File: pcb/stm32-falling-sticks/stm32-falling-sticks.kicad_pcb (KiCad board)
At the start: 2 copper layers, 112 x 87 mm, 73 parts, among them J1 MAG_01-05_OUT, J10 Barrel_Jack, J11 BUZ_OUT, J2 HAL_01-05_IN, J3 LCD_OUT, J4 MAG_06-10_OUT, J5 HAL_06-10_IN, J6 START_IN, J7 POT_IN, J8 MP1584EN, J9 Screw_Terminal_01x02, Q1 AO3400A, Q10 AO3400A, Q11 AO3400A, Q2 AO3400A, Q3 AO3400A, Q4 AO3400A, Q5 AO3400A, Q6 AO3400A, Q7 AO3400A, Q8 AO3400A, Q9 AO3400A, U1 YAAJ_BluePill_Part_Like_SWD_B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

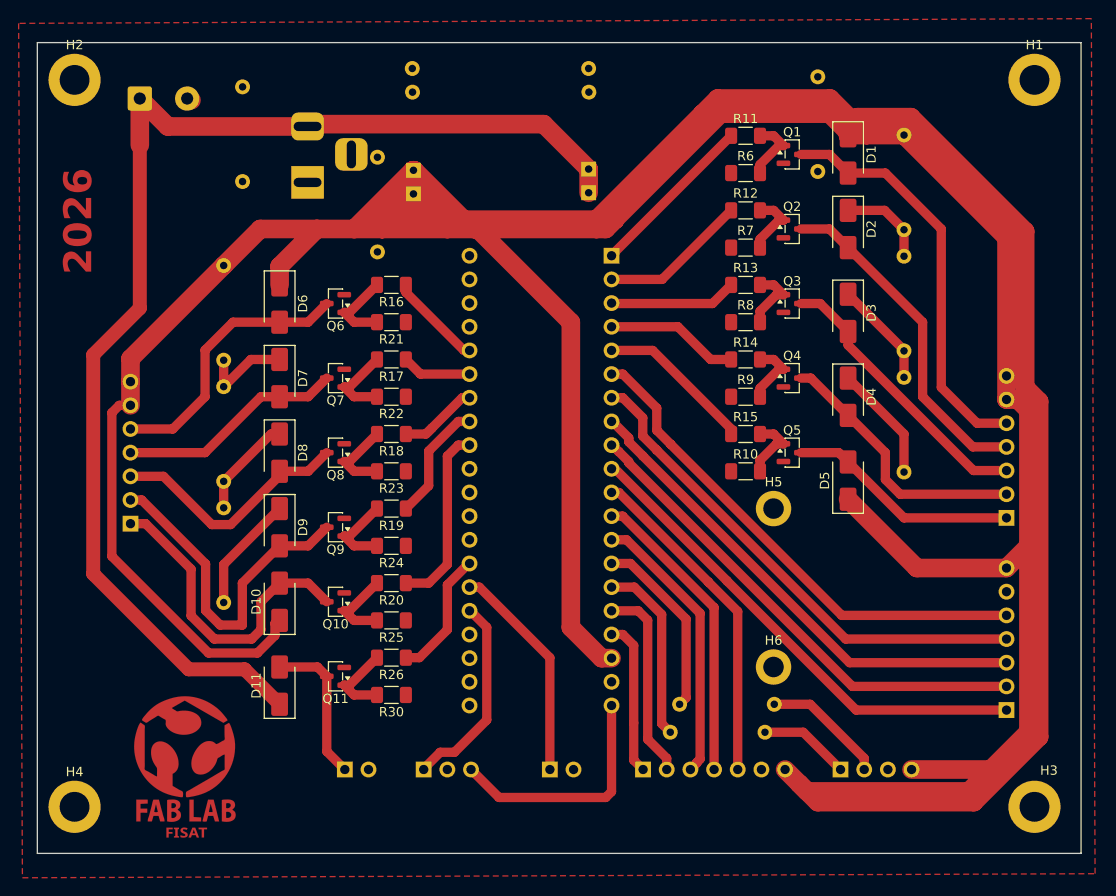
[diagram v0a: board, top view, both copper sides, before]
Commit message: fix(Fixed_12v_tracks): Fixed 12v tracks for electromagnet
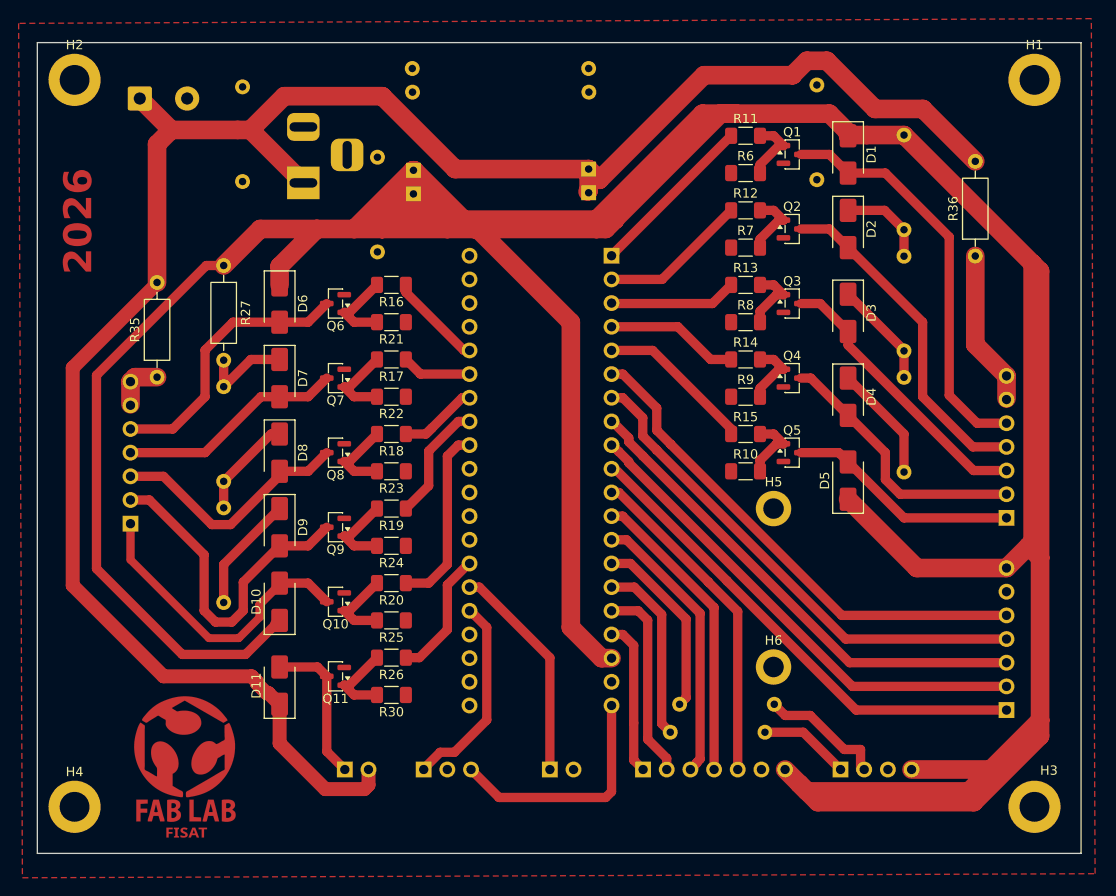
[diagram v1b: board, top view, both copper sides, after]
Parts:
- removed J10: Barrel_Jack, Connector_BarrelJack:BarrelJack_Horizontal
- added J12: Barrel_Jack_MountingPin, Connector_BarrelJack:BarrelJack_Horizontal, B.Cu at (120.5, 74.0)
- added R35: 0, Resistor_THT:R_Axial_DIN0207_L6.3mm_D2.5mm_P10.16mm_Horizontal, F.Cu at (104.8, 94.9)
- added R36: 0, Resistor_THT:R_Axial_DIN0207_L6.3mm_D2.5mm_P10.16mm_Horizontal, F.Cu at (192.7, 81.9)
- R27: moved to F.Cu
- moved R32 0.89 mm to (175.7, 63.5)
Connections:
- net /BUZ_OUT renamed /BUZ_GND
- J1 pad 6: +5V -> +12V
- J1 pad 7: +5V -> +12V
- J11 pad 2: GND -> +12V
- J4 pad 6: +5V -> +12V
- J4 pad 7: +5V -> +12V
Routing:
- net +12V: track 132.9 -> 237.2 mm
- net +5V: track 545.5 -> 484.9 mm
- net /MAG_10: track 34.2 -> 32.6 mm
- net GND: track 0.72 -> 0.00 mm
- net Net-(J3-Pin_2): track 13.3 -> 13.8 mm
- net /MAG_09: track 36.5 -> 36.0 mm

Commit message: feat(solder_mask_expansion): improve solder mask expansion
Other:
- rule pad_to_mask_clearance: 0 -> 0.2

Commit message: fix(jumper_fixes): jumper fixes
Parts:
- R27, R35, R36: moved to B.Cu

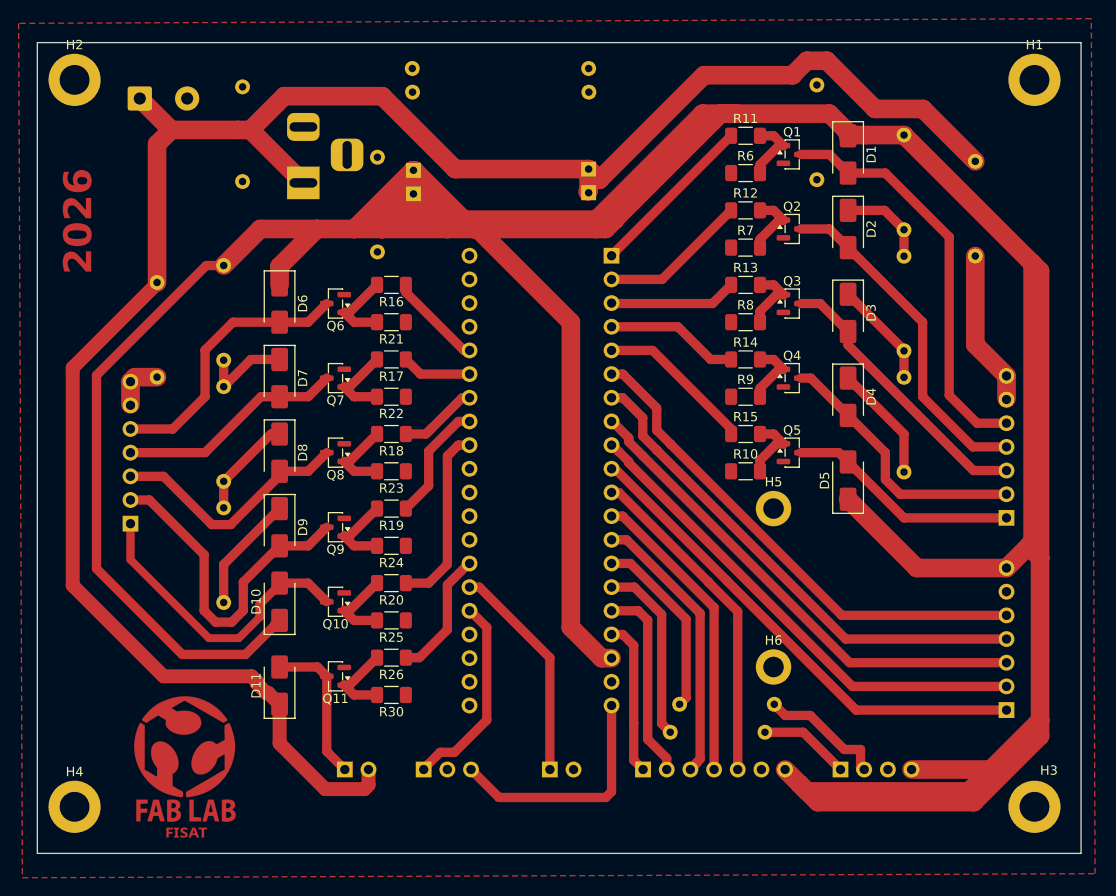
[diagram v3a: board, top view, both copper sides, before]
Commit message: Changed 12v tracks to 5v
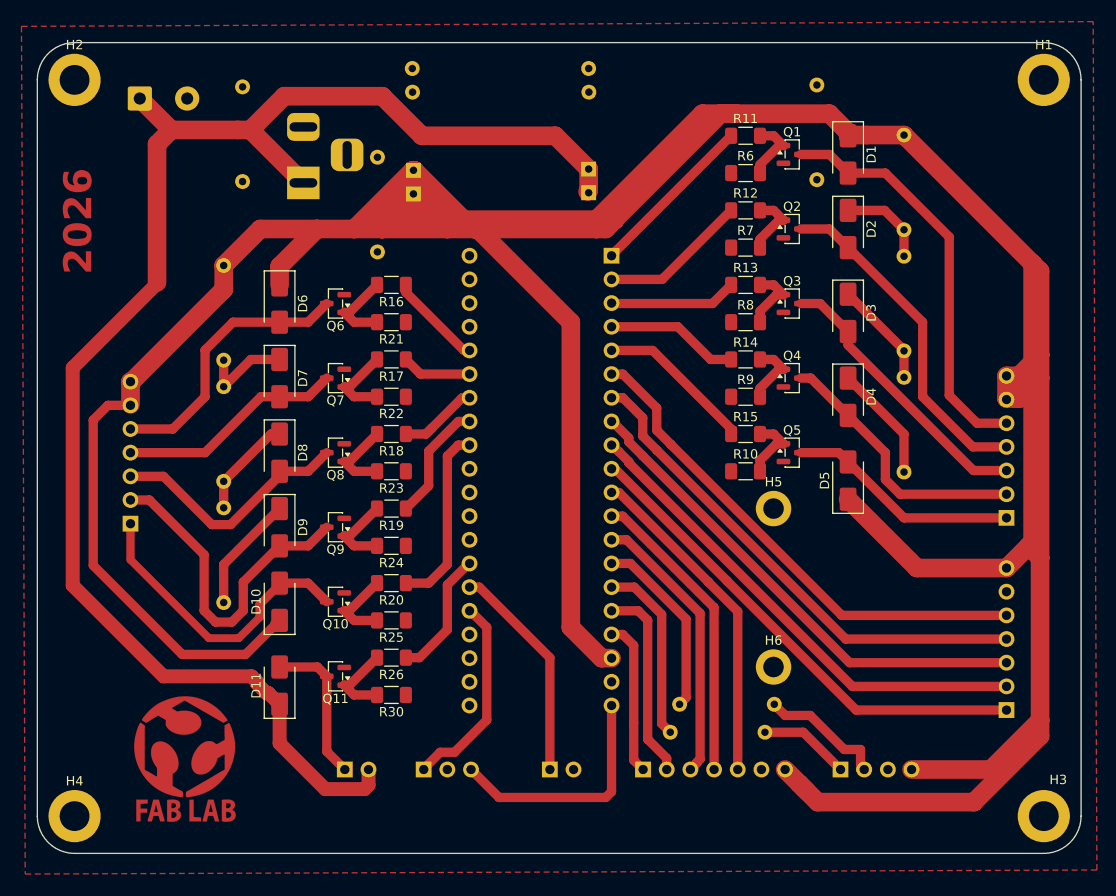
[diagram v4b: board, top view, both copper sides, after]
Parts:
- removed R35, R36: 0, Resistor_THT:R_Axial_DIN0207_L6.3mm_D2.5mm_P10.16mm_Horizontal
- moved H3 1.41 mm to (200.0, 142.0)
- moved H1 1.00 mm to (200.0, 63.0)
- moved H4 1.00 mm to (96.0, 142.0)
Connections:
- J1 pad 6: +12V -> +5V
- J1 pad 7: +12V -> +5V
- J4 pad 6: +12V -> +5V
- J4 pad 7: +12V -> +5V
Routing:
- net +12V: track 237.2 -> 163.3 mm
- net +5V: track 484.9 -> 478.8 mm
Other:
- outline, holes or cut-outs redrawn

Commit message: fix(Gerber_regenerated): Gerber_regenerated
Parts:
- added R35: 0, Resistor_THT:R_Axial_DIN0207_L6.3mm_D2.5mm_P10.16mm_Horizontal, F.Cu at (105.9, 83.2)
- added R36: 0, Resistor_THT:R_Axial_DIN0207_L6.3mm_D2.5mm_P10.16mm_Horizontal, F.Cu at (194.0, 82.6)
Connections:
- J1 pad 6: +5V -> +12V
- J1 pad 7: +5V -> +12V
- J4 pad 6: +5V -> +12V
- J4 pad 7: +5V -> +12V
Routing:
- net +12V: track 163.3 -> 241.2 mm
- net +5V: track 478.8 -> 466.8 mm
